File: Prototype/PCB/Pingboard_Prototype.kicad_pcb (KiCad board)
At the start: 2 copper layers, 92.7 x 22.9 mm, 23 parts, among them J1 Conn_01x02, J2 Conn_01x04, J3 Conn_01x02, SW1 SW_Push, SW2 SW_Push, SW3 SW_Push, SW4 SW_Push, U1 TLC59108xPW, U2 TLC59108xPW

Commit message: Draft 2
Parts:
- removed the SW1 at (115.6, 57.1)
- added D5: gn, LED_SMD:LED_0603_1608Metric_Pad1.05x0.95mm_HandSolder, F.Cu at (96.1, 52.7)
- added R7: 580, Resistor_SMD:R_0603_1608Metric_Pad0.98x0.95mm_HandSolder, F.Cu at (96.2, 50.8)
- C3: footprint Capacitor_SMD:C_0201_0603Metric_Pad0.64x0.40mm_HandSolder -> Capacitor_SMD:C_0603_1608Metric_Pad1.08x0.95mm_HandSolder
- J1: moved to B.Cu
- R5, R6: value 720 -> Rext
- moved C3 0.64 mm to (104.1, 55.2)
- turned J1 to 0 degrees
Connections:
- R4 pad 2: (no net) -> Switch4
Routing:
- net VCC: track 122.8 -> 153.4 mm
- net Switch4: track 77.6 -> 80.2 mm
- net Net-(D5-Pad2): track 0.00 -> 1.97 mm
- added copper zone on B.Cu, net GND
- added copper zone on F.Cu, net GND
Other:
- board size 92.7 x 22.9 mm -> 92.7 x 25.4 mm
- net class Default: clearance 0.2 -> 0.1524; trace_width 0.25 -> 0.1524; via_dia 0.8 -> 0.6858; via_drill 0.4 -> 0.3302
- net class VCC added: clearance 0.2032, trace_width 0.3048, via_dia 0.6858, via_drill 0.3302
- rule trace_clearance: 0.2 -> 0.1524
- rule trace_min: 0.2 -> 0.1524
- rule via_min_size: 0.4 -> 0.3302

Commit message: Draft 3
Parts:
- C3: moved to F.Cu
- J1, J3: footprint Connector_PinHeader_2.54mm:PinHeader_1x02_P2.54mm_Vertical -> Connector_PinHeader_1.27mm:PinHeader_1x02_P1.27mm_Vertical; moved to F.Cu
- J2: footprint Connector_PinHeader_2.54mm:PinHeader_1x04_P2.54mm_Vertical -> Connector_PinHeader_1.27mm:PinHeader_1x04_P1.27mm_Vertical; moved to F.Cu
- moved J1 19.0 mm to (107.3, 43.2), turned to 90 degrees
- moved J3 18.9 mm to (114.3, 43.2), turned to 90 degrees
- moved R7 14.7 mm to (110.5, 47.3), turned to 90 degrees
- moved D5 12.6 mm to (108.0, 48.3)
- moved J2 12.3 mm to (107.3, 61.0), turned to 90 degrees
- moved C3 9.67 mm to (108.0, 46.4), turned to 180 degrees
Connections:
- D5 pad 1: VCC -> GND
- R7 pad 1: GND -> Net-(D5-Pad2)
- R7 pad 2: Net-(D5-Pad2) -> VCC
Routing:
- net SCL: track 69.2 -> 53.1 mm
- net SDA: track 68.0 -> 54.5 mm
- net Switch4: track 80.2 -> 69.6 mm
- net Switch3: track 61.1 -> 51.1 mm
- net Switch2: track 40.9 -> 31.4 mm
- net Switch1: track 20.5 -> 12.5 mm
- net VCC: track 153.4 -> 150.0 mm
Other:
- board size 92.7 x 25.4 mm -> 87.6 x 25.4 mm
- board text added: "+5V"
- board text added: "GND"
- board text added: "PingBoard Rev 1 (c) PingTech GmbH 2020"
- board text added: "SCL"
- board text added: "SDA"
- board text added: "SW1"
- board text added: "SW2"
- board text added: "SW3"
- board text added: "SW4"

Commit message: Draft 4
Arduino Huckepack
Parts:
- removed D5: gn, LED_SMD:LED_0603_1608Metric_Pad1.05x0.95mm_HandSolder
- removed J3: Conn_01x02, Connector_PinHeader_1.27mm:PinHeader_1x02_P1.27mm_Vertical
- removed R7: 580, Resistor_SMD:R_0603_1608Metric_Pad0.98x0.95mm_HandSolder
- J1: value Conn_01x02 -> Conn_01x12; footprint Connector_PinHeader_1.27mm:PinHeader_1x02_P1.27mm_Vertical -> Connector_PinHeader_2.54mm:PinHeader_1x12_P2.54mm_Vertical
- J2: value Conn_01x04 -> Conn_01x12; footprint Connector_PinHeader_1.27mm:PinHeader_1x04_P1.27mm_Vertical -> Connector_PinHeader_2.54mm:PinHeader_1x12_P2.54mm_Vertical
- moved C3 13.8 mm to (102.6, 59.1), turned to 0 degrees
- moved J1 5.85 mm to (101.6, 41.9)
- moved J2 5.85 mm to (101.6, 62.2)
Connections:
- J1 pad 1: GND -> (no net)
- J1 pad 2: VCC -> (no net)
- J2 pad 1: Switch1 -> VCC
- J2 pad 2: Switch2 -> GND
- J2 pad 3: Switch3 -> (no net)
- J2 pad 4: Switch4 -> (no net)
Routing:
- net Switch4: track 69.6 -> 51.7 mm
- net Switch3: track 51.1 -> 34.5 mm
- net Switch2: track 31.4 -> 16.1 mm
- net Switch1: track 12.5 -> 9.25 mm
- net SDA: track 54.5 -> 56.8 mm
- net VCC: track 150.0 -> 148.1 mm
- net SCL: track 53.1 -> 54.8 mm
- net Net-(D5-Pad2): track 1.70 -> 0.00 mm
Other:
- board text added: "8"
- board text added: "9"

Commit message: Draft 5
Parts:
- added U3: 74LVC1G10, Package_TO_SOT_SMD:SOT-363_SC-70-6_Handsoldering, F.Cu at (144.1, 57.8)
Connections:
- J2 pad 3: (no net) -> RST
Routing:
- net RST: track 0.00 -> 39.9 mm
- net Switch1: track 9.25 -> 36.0 mm
- net GND: track 0.00 -> 8.84 mm, vias 0 -> 3
- net VCC: track 148.1 -> 156.3 mm
- net Switch2: track 16.1 -> 23.4 mm
- net Switch3: track 34.5 -> 37.6 mm
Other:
- board text added: "RST"

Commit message: Prototyp PCB Rev 1
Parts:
- moved C3 9.71 mm to (112.2, 57.1)
- moved J1 9.53 mm to (111.1, 41.9)
- moved J2 9.53 mm to (111.1, 62.2)
- moved C2 0.81 mm to (162.3, 54.0)
- moved C1 0.76 mm to (121.8, 54.0)
- moved R3 0.51 mm to (159.8, 57.1)
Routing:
- net Switch1: track 36.0 -> 49.2 mm
- net RST: track 39.9 -> 29.1 mm
- net Switch3: track 37.6 -> 27.6 mm
- net Switch4: track 51.7 -> 42.2 mm
- net Switch2: track 23.4 -> 16.1 mm
- net VCC: track 156.3 -> 152.2 mm
- net SCL: track 54.8 -> 57.9 mm
- net GND: vias 3 -> 1

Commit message: Set Rext for LED current based on datasheet
Using default values, Rext for 20 mA is 600 Ohm. We're using 520 Ohm
for a safety margin.
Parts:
- R5, R6: value Rext -> 520

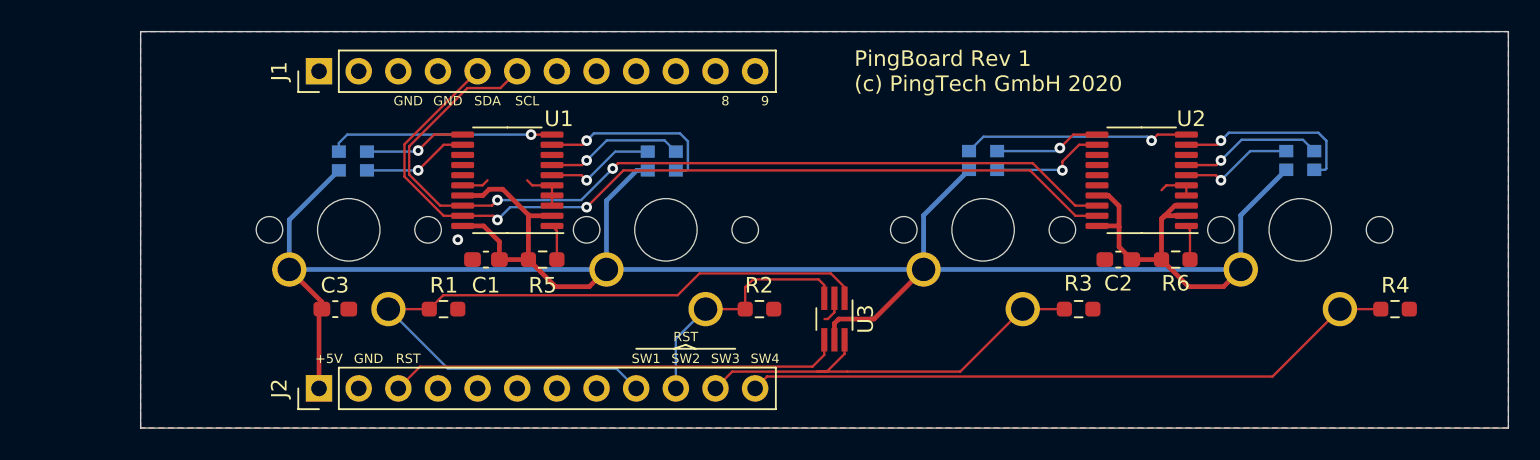
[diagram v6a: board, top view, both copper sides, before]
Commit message: Connect LED Driver reset to uC
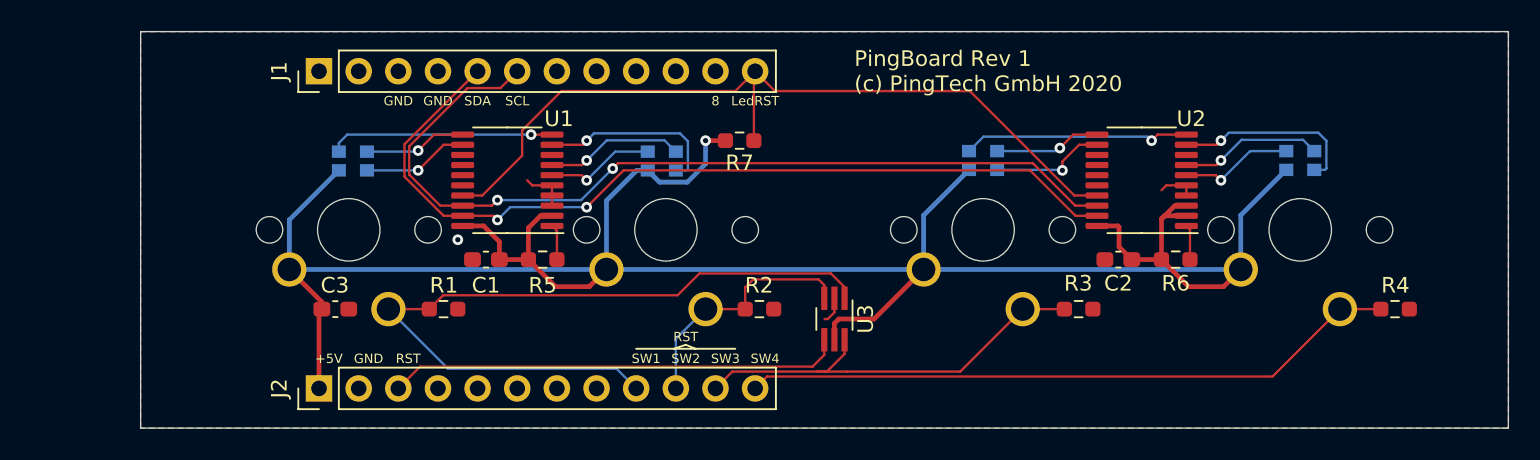
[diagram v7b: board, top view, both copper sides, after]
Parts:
- added R7: 4k7, Resistor_SMD:R_0603_1608Metric_Pad0.98x0.95mm_HandSolder, F.Cu at (138.1, 46.4)
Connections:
- J1 pad 12: (no net) -> LedRST
- U1 pad 17: VCC -> LedRST
- U2 pad 17: VCC -> LedRST
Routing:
- net LedRST: track 0.00 -> 52.7 mm
- net GND: track 8.84 -> 7.11 mm
- net VCC: track 152.2 -> 150.6 mm, vias 0 -> 1
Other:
- board text added: "LedRST"
- board text removed: "9"

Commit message: fix connection of REXT
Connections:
- J1 pad 1: (no net) -> Net-(J1-Pad1)
- J1 pad 10: (no net) -> Net-(J1-Pad10)
- J1 pad 11: (no net) -> Net-(J1-Pad11)
- J1 pad 2: (no net) -> Net-(J1-Pad2)
- J1 pad 7: (no net) -> Net-(J1-Pad7)
- J1 pad 8: (no net) -> Net-(J1-Pad8)
- J1 pad 9: (no net) -> Net-(J1-Pad9)
- J2 pad 4: (no net) -> Net-(J2-Pad4)
- J2 pad 5: (no net) -> Net-(J2-Pad5)
- J2 pad 6: (no net) -> Net-(J2-Pad6)
- J2 pad 7: (no net) -> Net-(J2-Pad7)
- J2 pad 8: (no net) -> Net-(J2-Pad8)
- R5 pad 2: VCC -> GND
- R6 pad 2: VCC -> GND
- U1 pad 14: (no net) -> Net-(U1-Pad14)
- U1 pad 15: (no net) -> Net-(U1-Pad15)
- U2 pad 14: (no net) -> Net-(U2-Pad14)
- U2 pad 15: (no net) -> Net-(U2-Pad15)
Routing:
- net VCC: track 150.6 -> 156.8 mm
